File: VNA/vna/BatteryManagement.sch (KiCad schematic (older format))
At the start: 0 parts

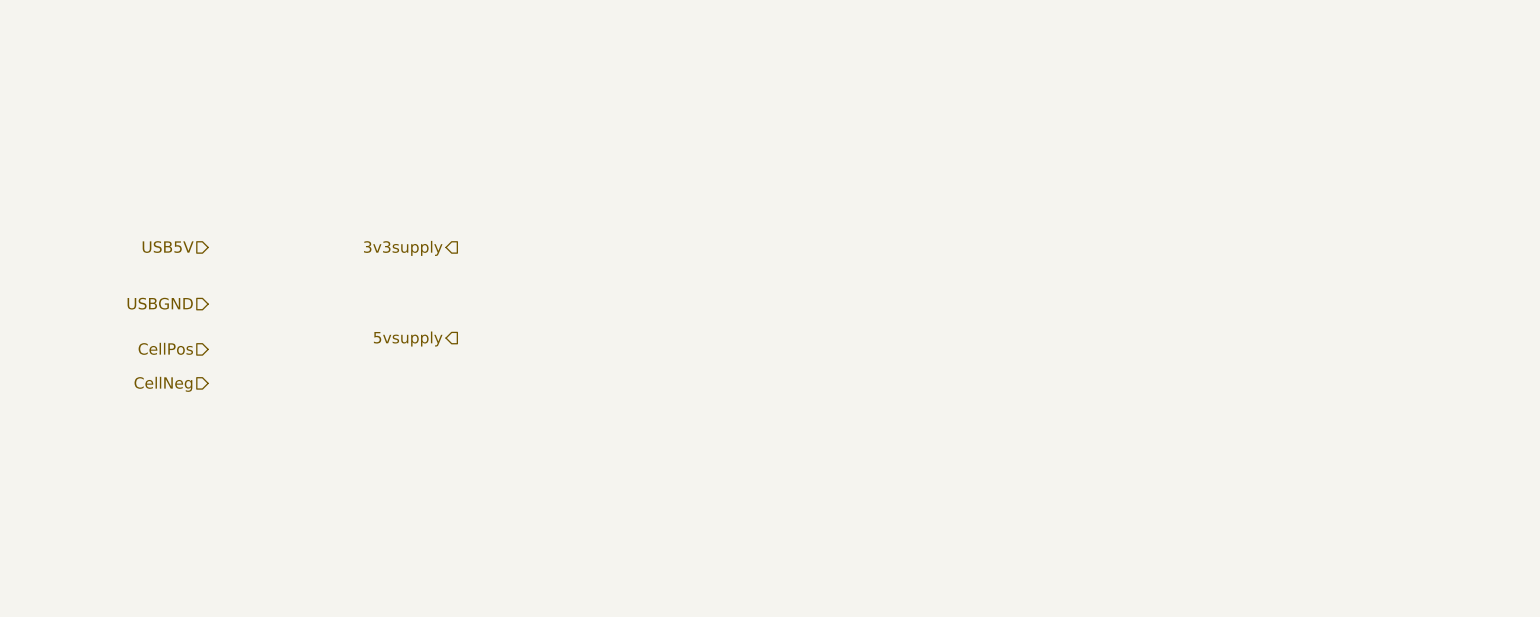
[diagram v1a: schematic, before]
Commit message: finished controller, chose compatible switches
controller and rf switches have been completed.

ToDo: finish filter design for RF Source, add auto gain control
ToDo: finish directional coupler footprints
ToDo: PCB Layout
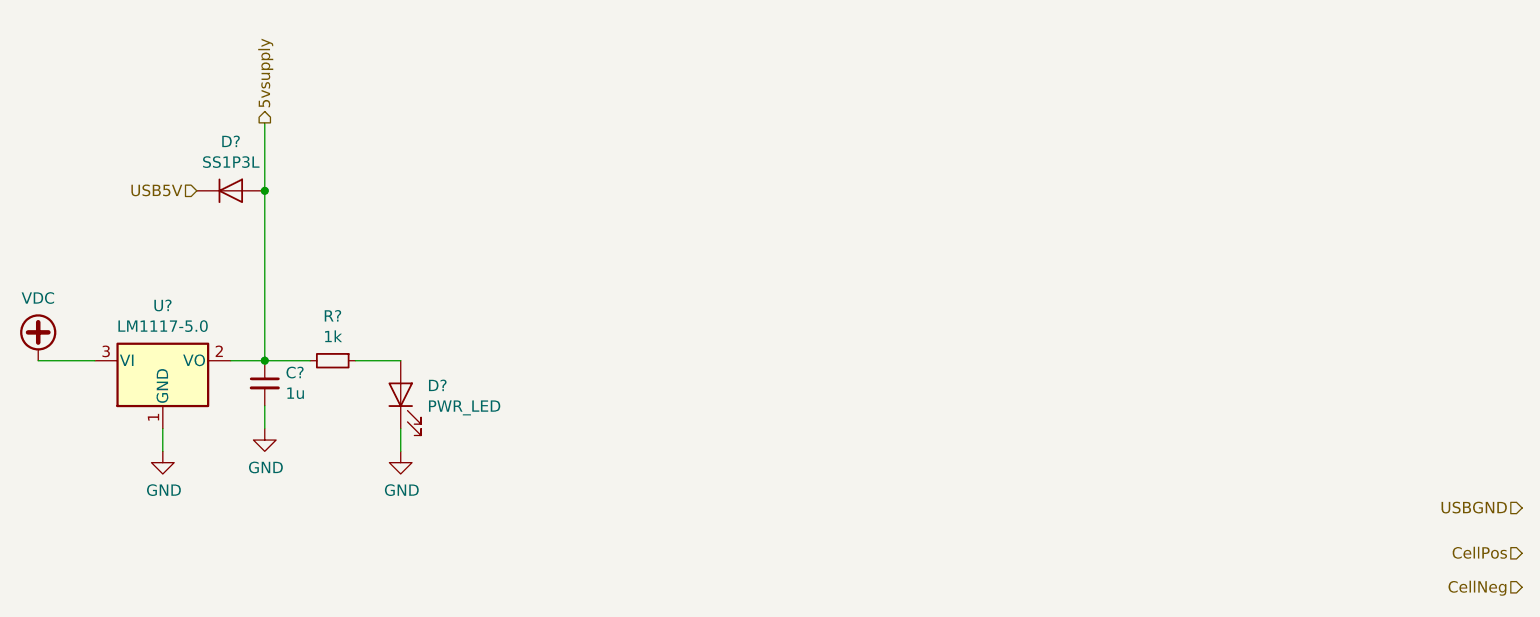
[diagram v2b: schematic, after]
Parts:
- added C?: 1u, symbol Device:C_Small
- added D?: PWR_LED, symbol Device:LED
- added D?: SS1P3L, symbol Device:D
- added R?: 1k, symbol Device:R_Small
- added U?: LM1117-5.0, symbol Regulator_Linear:LM1117-5.0
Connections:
- net 5vsupply: now also C?.1, D?.2 (A), R?.2, U?.2 (VO)
- net USB5V: now also D?.1 (K)
- new net: D?.2 (A), R?.1
- new net GND: C?.2, D?.1 (K), U?.1 (GND)
- new net VDC: U?.3 (VI)
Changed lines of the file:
@@
 $Descr A4 11693 8268
 encoding utf-8
-Sheet 10 10
+Sheet 7 10
 Title ""
 Date ""
@@
 Comment4 ""
 $EndDescr
-Text HLabel 2100 2100 0    50   Input ~ 0
+Text HLabel 2050 1850 0    50   Input ~ 0
 USB5V
-Text HLabel 2100 2350 0    50   Input ~ 0
+Text HLabel 7900 3250 0    50   Input ~ 0
 USBGND
-Text HLabel 3200 2100 0    50   Output ~ 0
-3v3supply
-Text HLabel 3200 2500 0    50   Output ~ 0
+Text HLabel 2350 1550 1    50   Output ~ 0
 5vsupply
-Text HLabel 2100 2550 0    50   Input ~ 0
+Text HLabel 7900 3450 0    50   Input ~ 0
 CellPos
-Text HLabel 2100 2700 0    50   Input ~ 0
+Text HLabel 7900 3600 0    50   Input ~ 0
 CellNeg
+$Comp
+L Regulator_Linear:LM1117-5.0 U?
+U 1 1 5DCCBE8D
+P 1900 2600
+F 0 "U?" H 1900 2842 50  0000 C CNN
+F 1 "LM1117-5.0" H 1900 2751 50  0000 C CNN
+F 2 "" H 1900 2600 50  0001 C CNN
+F 3 "http://www.ti.com/lit/ds/symlink/lm1117.pdf" H 1900 2600 50  0001 C CNN
+	1    1900 2600
+	1    0    0    -1
+$EndComp
+Wire Wire Line
+	2200 2600 2350 2600
+$Comp
+L Device:R_Small R?
+U 1 1 5DCCFC52
+P 2650 2600
+F 0 "R?" V 2454 2600 50  0000 C CNN
+F 1 "1k" V 2545 2600 50  0000 C CNN
+F 2 "" H 2650 2600 50  0001 C CNN
+F 3 "~" H 2650 2600 50  0001 C CNN
+	1    2650 2600
+	0    1    1    0
+$EndComp
+Wire Wire Line
+	2350 2600 2550 2600
+Connection ~ 2350 2600
+$Comp
+L Device:LED D?
+U 1 1 5DCD1460
+P 2950 2750
+F 0 "D?" V 2989 2632 50  0000 R CNN
+F 1 "PWR_LED" V 2898 2632 50  0000 R CNN
+F 2 "" H 2950 2750 50  0001 C CNN
+F 3 "~" H 2950 2750 50  0001 C CNN
+	1    2950 2750
+	0    -1   -1   0
+$EndComp
+Wire Wire Line
+	2750 2600 2950 2600
+$Comp
+L power:GND #PWR?
+U 1 1 5DCD2744
+P 2950 3000
+F 0 "#PWR?" H 2950 2750 50  0001 C CNN
+F 1 "GND" H 2955 2827 50  0000 C CNN
+F 2 "" H 2950 3000 50  0001 C CNN
+F 3 "" H 2950 3000 50  0001 C CNN
+	1    2950 3000
+	1    0    0    -1
+$EndComp
+$Comp
+L Device:C_Small C?
+U 1 1 5DCD33FA
+P 2350 2700
+F 0 "C?" H 2442 2746 50  0000 L CNN
+F 1 "1u" H 2442 2655 50  0000 L CNN
+F 2 "" H 2350 2700 50  0001 C CNN
+F 3 "~" H 2350 2700 50  0001 C CNN
+	1    2350 2700
+	1    0    0    -1
+$EndComp
+Wire Wire Line
+	2950 2900 2950 3000
+$Comp
+L power:GND #PWR?
+U 1 1 5DCD4771
+P 2350 2900
+F 0 "#PWR?" H 2350 2650 50  0001 C CNN
+F 1 "GND" H 2355 2727 50  0000 C CNN
+F 2 "" H 2350 2900 50  0001 C CNN
+F 3 "" H 2350 2900 50  0001 C CNN
+	1    2350 2900
+	1    0    0    -1
+$EndComp
+Wire Wire Line
+	2350 2800 2350 2900
+$Comp
+L power:GND #PWR?
+U 1 1 5DCD50B5
+P 1900 3000
+F 0 "#PWR?" H 1900 2750 50  0001 C CNN
+F 1 "GND" H 1905 2827 50  0000 C CNN
+F 2 "" H 1900 3000 50  0001 C CNN
+F 3 "" H 1900 3000 50  0001 C CNN
+	1    1900 3000
+	1    0    0    -1
+$EndComp
+Wire Wire Line
+	1900 2900 1900 3000
+Wire Wire Line
+	2350 1550 2350 1850
+$Comp
+L Device:D D?
+U 1 1 5DCD6860
+P 2200 1850
+F 0 "D?" H 2200 2066 50  0000 C CNN
+F 1 "SS1P3L" H 2200 1975 50  0000 C CNN
+F 2 "" H 2200 1850 50  0001 C CNN
+F 3 "~" H 2200 1850 50  0001 C CNN
+	1    2200 1850
+	1    0    0    -1
+$EndComp
+Connection ~ 2350 1850
+Wire Wire Line
+	2350 1850 2350 2600
+$Comp
+L power:VDC #PWR?
+U 1 1 5DCD8C22
+P 1350 2600
+F 0 "#PWR?" H 1350 2500 50  0001 C CNN
+F 1 "VDC" H 1350 2875 50  0000 C CNN
+F 2 "" H 1350 2600 50  0001 C CNN
+F 3 "" H 1350 2600 50  0001 C CNN
+	1    1350 2600
+	1    0    0    -1
+$EndComp
+Wire Wire Line
+	1350 2600 1600 2600
 $EndSCHEMATC
